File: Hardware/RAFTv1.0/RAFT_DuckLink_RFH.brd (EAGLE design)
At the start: 73.7 x 83.8 mm, 145 parts, among them J1 AMPHENOL_132134, J2 AMPHENOL_132134, J4 Micro-USB, J5 132134-15, J6 S2B-PH-K-S(LF)(SN), J8 POWER_JACK, Q1 SIA817EDJ, Q2 SI7288DP, Q4 SI7288DP, U1 SX1276, U10 PE4259, U2 MAX2771ETI+, U3 ESP32-D0WD, U4 W25Q16BVSSIG, U5 INTERFACE-CP2102-GMR(QFN28), U6 PE4259, U7 SP0503BAHT, U8 BQ24650RVAR, U9 TPS63070RNMT, Y1 32.768kHz

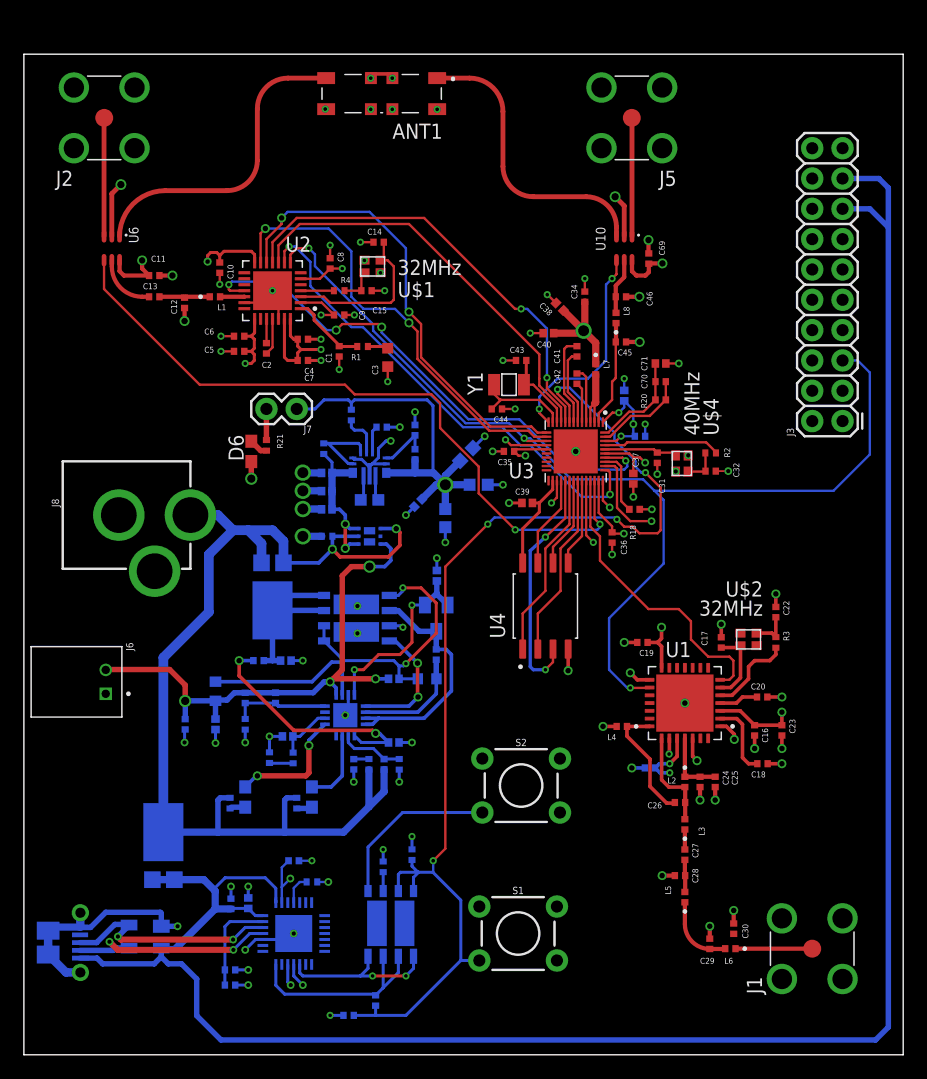
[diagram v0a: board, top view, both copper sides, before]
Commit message: complete routing
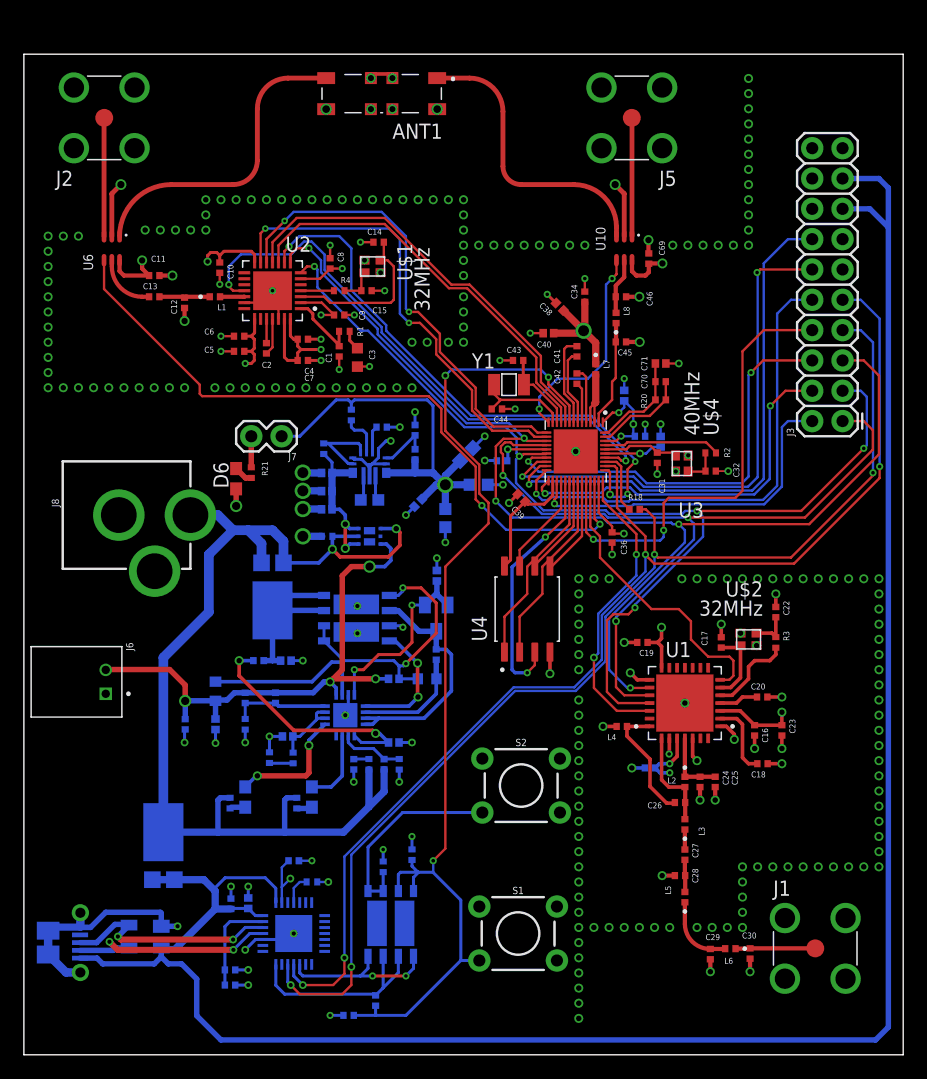
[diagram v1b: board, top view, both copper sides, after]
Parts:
- moved C37 3.85 mm to (53.3, 51.4), flipped to the bottom, turned to 90 degrees
- moved D6 2.62 mm to (17.8, 48.3)
- moved R21 2.62 mm to (19.1, 48.8)
- moved J7 2.62 mm to (21.6, 51.8)
- moved C3 2.54 mm to (27.9, 58.4)
- moved C30 2.49 mm to (60.8, 8.48), turned to 90 degrees
- moved R1 1.98 mm to (26.8, 60.6)
- moved U4 1.55 mm to (42.2, 37.3)
- moved C35 0.98 mm to (40.1, 49.8), flipped to the bottom, turned to 180 degrees
- moved C29 0.87 mm to (57.5, 8.43), turned to 90 degrees
- moved C39 0.65 mm to (41.7, 46.7), turned to 315 degrees
- moved J1 0.26 mm to (66.3, 8.92)
- moved C43 0.25 mm to (41.4, 58.2)
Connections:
- net GPIO0: now also J3.14; no longer J3.2
- net GPIO15: now also J3.6; no longer J3.10
- net GPIO16: now also J3.4; no longer J3.12
- net GPIO17: now also J3.2; no longer J3.14
- net GPIO2: now also J3.12; no longer J3.4
- net GPIO3: now also J3.10; no longer J3.6
- net U0RXD: now also J3.9; no longer J3.7
- net U0TXD: now also J3.7; no longer J3.9
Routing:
- net U0TXD: track 2.84 -> 97.1 mm, vias 2 -> 4
- net SPI_MOSI: track 0.00 -> 94.1 mm, vias 0 -> 5
- net U0RXD: track 9.80 -> 103.8 mm, vias 2 -> 4
- net SPI_MISO: track 3.62 -> 66.1 mm, vias 1 -> 3
- net GPIO0: track 0.00 -> 45.9 mm, vias 0 -> 1
- net GPIO2: track 0.00 -> 44.8 mm, vias 0 -> 2
- net GPIO3: track 0.00 -> 41.4 mm, vias 0 -> 1
- net GPIO15: track 0.00 -> 35.5 mm, vias 0 -> 2
- net GPIO4: track 5.42 -> 39.4 mm, vias 1 -> 2
- net GPIO16: track 0.00 -> 31.4 mm, vias 0 -> 2
- net GPIO17: track 2.06 -> 29.6 mm
- net SX_CS: track 2.48 -> 25.5 mm, vias 1 -> 2
- net SPI_CLK: track 92.8 -> 101.7 mm, vias 3 -> 5
- net GPS_CS: track 40.7 -> 48.1 mm, vias 2 -> 4
- net CHIP_PU: track 94.9 -> 87.6 mm, vias 5 -> 3
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
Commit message: fixed issue
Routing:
- net N$36: track 8.60 -> 9.34 mm
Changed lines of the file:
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@@
 <wire x1="23.188" y1="63.008" x2="24.952" y2="63.008" width="0.2" layer="1" grouprefs="GPS"/>
 <wire x1="24.952" y1="63.008" x2="25.984" y2="61.976" width="0.2" layer="1" grouprefs="GPS"/>
-<wire x1="47.9044" y1="58.039" x2="47.9044" y2="57.8614" width="0.2" layer="1" grouprefs="MCU"/>
 <wire x1="50.292" y1="54.7806" x2="51.054" y2="54.0186" width="0.2" layer="16" grouprefs="MCU"/>
 <wire x1="51.054" y1="54.0186" x2="51.054" y2="52.832" width="0.2" layer="16" grouprefs="MCU"/>
@@
 <wire x1="46.8884" y1="60.6552" x2="46.6852" y2="60.452" width="0.6096" layer="1" grouprefs="MCU"/>
 <wire x1="46.6852" y1="60.452" x2="44.381" y2="60.452" width="0.6096" layer="1" grouprefs="MCU"/>
-<wire x1="47.9044" y1="57.8614" x2="47.9044" y2="59.6392" width="0.6096" layer="1" grouprefs="MCU"/>
 <wire x1="47.9044" y1="59.6392" x2="46.8884" y2="60.6552" width="0.6096" layer="1" grouprefs="MCU"/>
 <wire x1="51.1808" y1="51.816" x2="51.054" y2="51.9428" width="0.2" layer="16" grouprefs="MCU"/>
@@
 <wire x1="46.8884" y1="60.6552" x2="45.194021875" y2="62.349578125" width="0.6096" layer="1"/>
 <wire x1="45.194021875" y1="62.349578125" x2="45.194021875" y2="62.353184375" width="0.6096" layer="1"/>
+<wire x1="47.9044" y1="57.8614" x2="47.9044" y2="59.6392" width="0.6096" layer="1"/>
 </signal>
 <signal name="TIME_SYNC">
@@
 <wire x1="6.716" y1="64.15" x2="6.716" y2="66.564" width="0.2" layer="1"/>
 <wire x1="48.26" y1="44.45" x2="47.7874" y2="43.9774" width="0.2" layer="16"/>
-<wire x1="47.7874" y1="43.9774" x2="40.3987" y2="43.9774" width="0.2" layer="16"/>
-<wire x1="40.3987" y1="43.9774" x2="38.3667" y2="46.0094" width="0.2" layer="16"/>
+<wire x1="39.90205" y1="44.47405" x2="38.3667" y2="46.0094" width="0.2" layer="16"/>
 <wire x1="37.846" y1="46.5301" x2="37.846" y2="49.276" width="0.2" layer="1"/>
 <wire x1="37.846" y1="49.276" x2="34.9714" y2="52.1506" width="0.2" layer="1"/>
@@
 <wire x1="14.732" y1="56.134" x2="6.716" y2="64.15" width="0.2" layer="1"/>
 <wire x1="33.9121625" y1="55.1728" x2="14.9312" y2="55.1728" width="0.2" layer="1"/>
+<wire x1="47.7874" y1="43.9774" x2="45.4306" y2="43.9774" width="0.2" layer="16"/>
+<wire x1="44.93395" y1="44.47405" x2="39.90205" y2="44.47405" width="0.2" layer="16"/>
+<wire x1="45.4306" y1="43.9774" x2="44.93395" y2="44.47405" width="0.2" layer="16"/>
 </signal>
 <signal name="GPS_INT_ANT">
@@
 <contactref element="U3" pad="30"/>
 <contactref element="U4" pad="1"/>
-<wire x1="45.703" y1="48.101" x2="45.703" y2="44.433" width="0.2" layer="1" grouprefs="MCU"/>
-<wire x1="45.703" y1="44.433" x2="42.164" y2="40.894" width="0.2" layer="1" grouprefs="MCU"/>
-<wire x1="42.164" y1="40.894" x2="42.164" y2="38.608" width="0.2" layer="1" grouprefs="MCU"/>
+<wire x1="45.703" y1="48.101" x2="45.703" y2="45.449" width="0.2" layer="1" grouprefs="MCU"/>
 <wire x1="42.164" y1="38.608" x2="40.259" y2="36.703" width="0.2" layer="1" grouprefs="MCU"/>
 <wire x1="40.259" y1="36.703" x2="40.259" y2="33.733" width="0.2" layer="1" grouprefs="MCU"/>
+<wire x1="45.703" y1="45.449" x2="44.704" y2="44.45" width="0.2" layer="1"/>
+<wire x1="44.4603625" y1="44.45" x2="42.164" y2="42.1536375" width="0.2" layer="1"/>
+<wire x1="44.704" y1="44.45" x2="44.4603625" y2="44.45" width="0.2" layer="1"/>
+<wire x1="42.164" y1="42.1536375" x2="42.164" y2="38.608" width="0.2" layer="1"/>
 </signal>
 <signal name="N$35">
 <contactref element="U3" pad="31"/>
 <contactref element="U4" pad="6"/>
-<wire x1="46.053" y1="48.101" x2="46.053" y2="44.275" width="0.2" layer="1" grouprefs="MCU"/>
-<wire x1="42.799" y1="41.021" x2="42.799" y2="40.943" width="0.2" layer="1" grouprefs="MCU"/>
-<wire x1="46.053" y1="44.275" x2="42.799" y2="41.021" width="0.2" layer="1" grouprefs="MCU"/>
+<wire x1="46.053" y1="48.101" x2="46.053" y2="45.291" width="0.2" layer="1" grouprefs="MCU"/>
+<wire x1="46.053" y1="45.291" x2="42.799" y2="42.037" width="0.2" layer="1"/>
+<wire x1="42.799" y1="42.037" x2="42.799" y2="40.943" width="0.2" layer="1"/>
 </signal>
 <signal name="N$36">
@@
 <contactref element="U4" pad="7"/>
 <wire x1="45.003" y1="48.101" x2="45.003" y2="45.765" width="0.2" layer="1" grouprefs="MCU"/>
-<wire x1="41.529" y1="42.291" x2="41.529" y2="40.943" width="0.2" layer="1" grouprefs="MCU"/>
-<wire x1="41.529" y1="42.291" x2="45.003" y2="45.765" width="0.2" layer="1" grouprefs="MCU"/>
+<wire x1="45.003" y1="45.765" x2="44.704" y2="45.466" width="0.2" layer="1"/>
+<wire x1="44.704" y1="45.466" x2="43.434" y2="45.466" width="0.2" layer="1"/>
+<wire x1="43.434" y1="45.466" x2="41.529" y2="43.561" width="0.2" layer="1"/>
+<wire x1="41.529" y1="43.561" x2="41.529" y2="40.943" width="0.2" layer="1"/>
 </signal>
 <signal name="N$37">
 <contactref element="U3" pad="29"/>
 <contactref element="U4" pad="3"/>
-<wire x1="45.353" y1="48.101" x2="45.353" y2="44.958" width="0.2" layer="1" grouprefs="MCU"/>
-<wire x1="45.353" y1="44.958" x2="43.688" y2="43.3702" width="0.2" layer="1" grouprefs="MCU"/>
-<via x="43.688" y="43.3702" extent="1-16" drill="0.3" grouprefs="MCU"/>
+<wire x1="45.353" y1="48.101" x2="45.353" y2="46.228" width="0.2" layer="1" grouprefs="MCU"/>
+<via x="42.672" y="43.6242" extent="1-16" drill="0.3" grouprefs="MCU"/>
 <via x="42.164" y="32.004" extent="1-16" drill="0.3" grouprefs="MCU"/>
+<wire x1="45.353" y1="46.228" x2="45.353" y2="46.180890625" width="0.2" layer="1" grouprefs="MCU"/>
 <wire x1="42.164" y1="32.004" x2="42.799" y2="32.639" width="0.2" layer="1" grouprefs="MCU"/>
 <wire x1="42.799" y1="32.639" x2="42.799" y2="33.733" width="0.2" layer="1" grouprefs="MCU"/>
-<wire x1="40.894" y1="32.258" x2="41.148" y2="32.004" width="0.2794" layer="16"/>
-<wire x1="41.148" y1="32.004" x2="42.164" y2="32.004" width="0.2794" layer="16"/>
-<wire x1="43.688" y1="43.3702" x2="40.894" y2="40.85691875" width="0.2794" layer="16" grouprefs="MCU"/>
-<wire x1="40.894" y1="40.85691875" x2="40.894" y2="32.258" width="0.2794" layer="16"/>
+<wire x1="42.672" y1="43.6242" x2="42.164" y2="43.1162" width="0.2" layer="16"/>
+<wire x1="42.164" y1="38.1" x2="40.894" y2="36.83" width="0.2" layer="16"/>
+<wire x1="40.894" y1="36.83" x2="40.894" y2="32.766" width="0.2" layer="16"/>
+<wire x1="41.656" y1="32.004" x2="42.164" y2="32.004" width="0.2" layer="16"/>
+<wire x1="42.164" y1="43.1162" x2="42.164" y2="38.1" width="0.2" layer="16"/>
+<wire x1="40.894" y1="32.766" x2="41.656" y2="32.004" width="0.2" layer="16"/>
+<wire x1="45.353" y1="46.180890625" x2="45.353" y2="45.607" width="0.2" layer="1"/>
+<wire x1="45.353" y1="45.607" x2="44.704" y2="44.958" width="0.2" layer="1"/>
+<wire x1="44.704" y1="44.958" x2="44.0058" y2="44.958" width="0.2" layer="1"/>
+<wire x1="44.0058" y1="44.958" x2="42.672" y2="43.6242" width="0.2" layer="1"/>
 </signal>
 <signal name="N$38">
 <contactref element="U3" pad="33"/>
 <contactref element="U4" pad="5"/>
-<wire x1="44.069" y1="40.943" x2="44.245" y2="40.943" width="0.2" layer="1" grouprefs="MCU"/>
-<wire x1="46.753" y1="43.451" x2="46.753" y2="48.101" width="0.2" layer="1" grouprefs="MCU"/>
-<wire x1="44.245" y1="40.943" x2="46.753" y2="43.451" width="0.2" layer="1" grouprefs="MCU"/>
+<wire x1="46.753" y1="44.467" x2="46.753" y2="48.101" width="0.2" layer="1" grouprefs="MCU"/>
+<wire x1="46.753" y1="44.467" x2="44.069" y2="41.783" width="0.2" layer="1"/>
+<wire x1="44.069" y1="40.943" x2="44.069" y2="41.783" width="0.2" layer="1" grouprefs="MCU"/>
 </signal>
 <signal name="N$39">
 <contactref element="U3" pad="32"/>
 <contactref element="U4" pad="2"/>
-<wire x1="46.403" y1="48.101" x2="46.403" y2="43.863" width="0.2" layer="1" grouprefs="MCU"/>
-<wire x1="43.434" y1="40.894" x2="43.434" y2="38.608" width="0.2" layer="1" grouprefs="MCU"/>
+<wire x1="46.403" y1="48.101" x2="46.403" y2="44.879" width="0.2" layer="1" grouprefs="MCU"/>
+<wire x1="43.434" y1="41.91" x2="43.434" y2="38.608" width="0.2" layer="1" grouprefs="MCU"/>
 <wire x1="43.434" y1="38.608" x2="41.529" y2="36.703" width="0.2" layer="1" grouprefs="MCU"/>
 <wire x1="41.529" y1="36.703" x2="41.529" y2="33.733" width="0.2" layer="1" grouprefs="MCU"/>
-<wire x1="46.403" y1="43.863" x2="43.434" y2="40.894" width="0.2" layer="1" grouprefs="MCU"/>
+<wire x1="46.403" y1="44.879" x2="43.434" y2="41.91" width="0.2" layer="1" grouprefs="MCU"/>
 </signal>
 <signal name="N$40">

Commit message: fixed one thing probably broke several others
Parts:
- moved C30 1.73 mm to (59.7, 7.19)
- moved C29 1.54 mm to (58.4, 7.19)
- moved S2 1.44 mm to (40.6, 21.5)
- moved S1 1.08 mm to (40.6, 9.40)
- moved L6 0.13 mm to (59.1, 8.89)
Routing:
- net GND: track 138.3 -> 277.5 mm, vias 101 -> 169
- net N$21: track 6.69 -> 8.26 mm
- net N$44: track 17.3 -> 15.9 mm
- net N$20: track 6.07 -> 7.06 mm
- net CHIP_PU: track 87.6 -> 87.0 mm
- added copper zone on layer 1, net GND

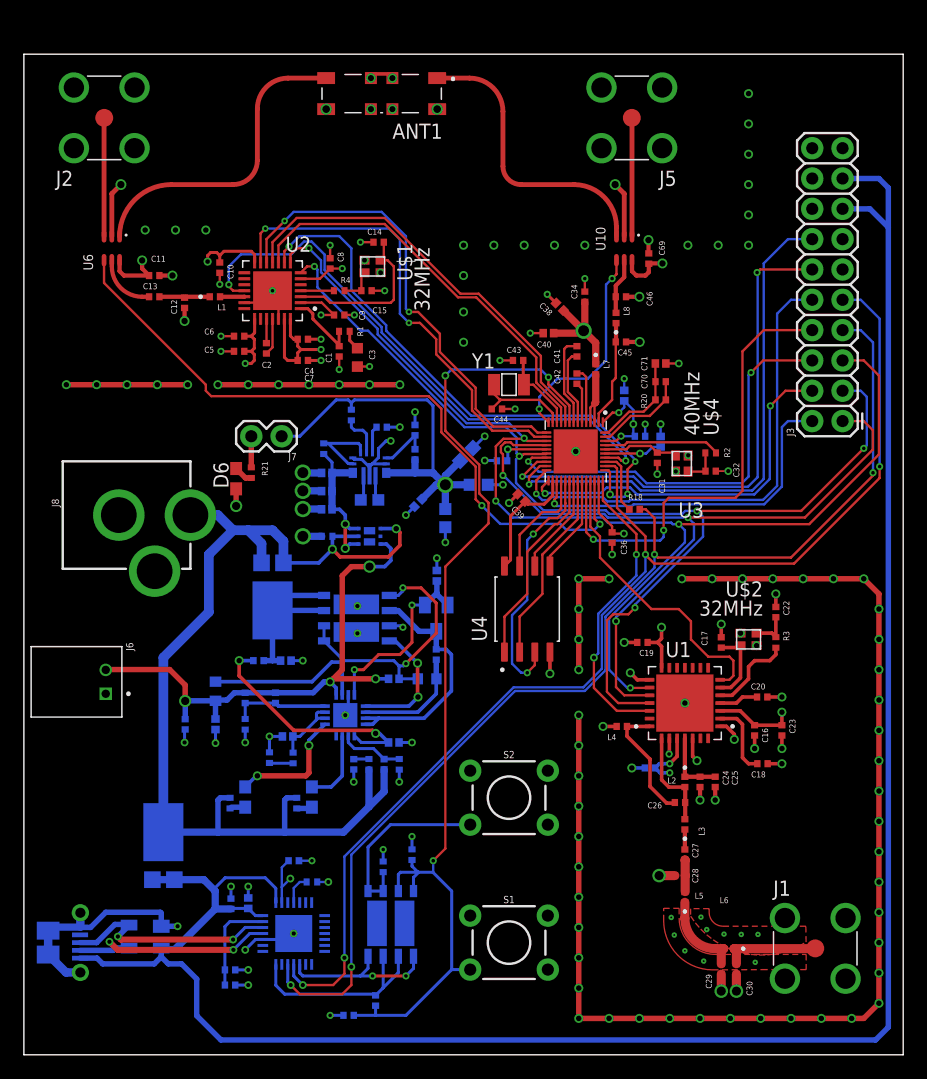
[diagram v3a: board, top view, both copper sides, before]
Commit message: pretty much final. added fuse and thermistor header
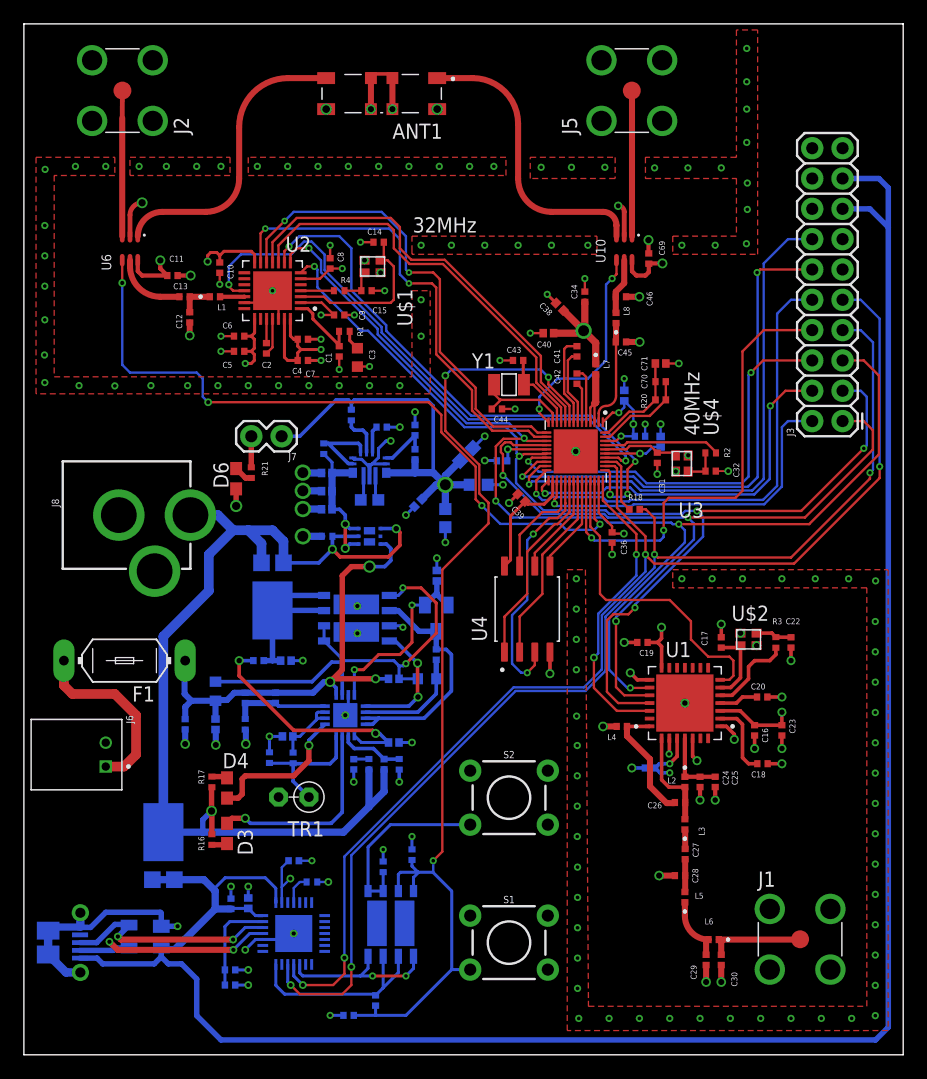
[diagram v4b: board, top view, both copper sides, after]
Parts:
- added F1: (no value), fuse:LITTLEFUSE
- added TR1: (no value), discrete:RS-2,5
- moved R16 7.74 mm to (15.7, 18.0), flipped to the top
- moved D3 7.74 mm to (17.0, 18.5), flipped to the top
- moved J6 6.10 mm to (6.86, 25.1)
- moved C22 2.84 mm to (64.3, 34.5), turned to 90 degrees
- moved J2 2.75 mm to (8.26, 80.8)
- moved C13 2.54 mm to (13.5, 63.5)
- moved R17 2.34 mm to (15.7, 22.9), flipped to the top, turned to 90 degrees
- moved J5 2.29 mm to (50.9, 80.8)
- moved D4 1.70 mm to (17.0, 22.4), flipped to the top, turned to 90 degrees
- moved U6 1.52 mm to (8.89, 67.6)
- moved C11 1.52 mm to (12.4, 65.3)
- moved C29 1.48 mm to (57.1, 7.95)
- moved L6 1.48 mm to (57.8, 9.65)
- moved J1 1.48 mm to (65.0, 9.68)
- moved C30 1.48 mm to (58.4, 7.95)
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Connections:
- new net N$56: F1.2, J6.1
- net GND: now also J6.2, TR1.2; no longer J6.1
- net PACK_THERM: now also TR1.1
- net V_BAT: now also F1.1; no longer J6.2
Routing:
- net GND: track 277.5 -> 141.6 mm, vias 169 -> 200
- net N$56: track 0.00 -> 15.4 mm
- net N$68: track 6.30 -> 16.8 mm, vias 0 -> 1
- net PACK_THERM: track 1.99 -> 11.1 mm
- net V_BAT: track 46.6 -> 41.4 mm, vias 4 -> 3
- net GPS_ANT_SEL: track 59.1 -> 61.9 mm, vias 2 -> 4
- net N$70: track 9.93 -> 12.2 mm
- net N$7: track 9.93 -> 12.2 mm
- net N$67: track 10.4 -> 12.5 mm, vias 2 -> 1
- net SX_RST: track 24.9 -> 26.7 mm
- net N$20: track 7.06 -> 5.30 mm
- net VIN: track 90.8 -> 89.3 mm, vias 2 -> 3
- net GPS_INT_ANT: track 25.3 -> 23.8 mm
- net N$8: track 4.28 -> 2.97 mm
- net TIME_SYNC: track 36.2 -> 37.3 mm
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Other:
- board size 73.7 x 83.8 mm -> 73.7 x 86.4 mm
